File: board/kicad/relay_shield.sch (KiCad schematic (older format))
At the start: 16 parts

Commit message: Changed repository layout and added converted Eagle files.
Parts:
- removed R?: 10K, ~, symbol R
- removed R?: 220, ~, symbol R
- removed U?: Optoisolator, ~, symbol PHDARL
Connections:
- wire segments 35 -> 30
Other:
- moved on the sheet: R?, SW?
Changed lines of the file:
@@
 LIBS:contrib
 LIBS:valves
+LIBS:spark_core
 LIBS:relay_shield-cache
 EELAYER 27 0
@@
 Sheet 1 1
 Title ""
-Date "13 aug 2013"
+Date "14 aug 2013"
 Rev ""
 Comp ""
@@
 L SPST SW?
 U 1 1 520A9B3C
-P 1250 1400
-F 0 "SW?" H 1250 1500 70  0000 C CNN
-F 1 "SPST" H 1250 1300 70  0000 C CNN
-F 2 "~" H 1250 1400 60  0000 C CNN
-F 3 "~" H 1250 1400 60  0000 C CNN
-	1    1250 1400
+P 3000 1400
+F 0 "SW?" H 3000 1500 70  0000 C CNN
+F 1 "SPST" H 3000 1300 70  0000 C CNN
+F 2 "~" H 3000 1400 60  0000 C CNN
+F 3 "~" H 3000 1400 60  0000 C CNN
+	1    3000 1400
 	0    -1   -1   0
 $EndComp
@@
 L +3.3V #PWR04
 U 1 1 520A9BBE
-P 1250 900
-F 0 "#PWR04" H 1250 860 30  0001 C CNN
-F 1 "+3.3V" H 1250 1010 30  0000 C CNN
-F 2 "" H 1250 900 60  0000 C CNN
-F 3 "" H 1250 900 60  0000 C CNN
-	1    1250 900
+P 3000 900
+F 0 "#PWR04" H 3000 860 30  0001 C CNN
+F 1 "+3.3V" H 3000 1010 30  0000 C CNN
+F 2 "" H 3000 900 60  0000 C CNN
+F 3 "" H 3000 900 60  0000 C CNN
+	1    3000 900
 	1    0    0    -1
 $EndComp
@@
 	8450 5300 8700 5300
 Wire Wire Line
-	1250 1900 1250 2550
-Wire Wire Line
 	3350 900  3350 1450
 Wire Wire Line
 	3800 1300 3800 1450
-Wire Wire Line
-	3250 2550 3500 2550
 Wire Wire Line
 	3800 2350 3350 2350
@@
 Wire Wire Line
 	3800 1450 4200 1450
-Wire Wire Line
-	2750 1300 3800 1300
 $Comp
 L +5V #PWR07
@@
 L R R?
 U 1 1 520AA4F9
-P 3000 2550
-F 0 "R?" V 3080 2550 40  0000 C CNN
-F 1 "1K" V 3007 2551 40  0000 C CNN
-F 2 "~" V 2930 2550 30  0000 C CNN
-F 3 "~" H 3000 2550 30  0000 C CNN
-	1    3000 2550
+P 3250 2550
+F 0 "R?" V 3330 2550 40  0000 C CNN
+F 1 "1K" V 3257 2551 40  0000 C CNN
+F 2 "~" V 3180 2550 30  0000 C CNN
+F 3 "~" H 3250 2550 30  0000 C CNN
+	1    3250 2550
 	0    -1   -1   0
 $EndComp
-$Comp
-L PHDARL U?
-U 1 1 520AA563
-P 2150 2350
-F 0 "U?" H 2160 2670 70  0000 C CNN
-F 1 "Optoisolator" H 2160 2030 70  0000 C CNN
-F 2 "~" H 2150 2350 60  0000 C CNN
-F 3 "~" H 2150 2350 60  0000 C CNN
-	1    2150 2350
-	1    0    0    -1
-$EndComp
-Wire Wire Line
-	2750 1300 2750 2150
-Connection ~ 3350 1300
-$Comp
-L R R?
-U 1 1 520AA5CD
-P 1550 2800
-F 0 "R?" V 1630 2800 40  0000 C CNN
-F 1 "220" V 1557 2801 40  0000 C CNN
-F 2 "~" V 1480 2800 30  0000 C CNN
-F 3 "~" H 1550 2800 30  0000 C CNN
-	1    1550 2800
-	1    0    0    -1
-$EndComp
-Wire Wire Line
-	1250 2450 850  2450
 Text Notes 8750 4250 0    30   ~ 0
 MCP1825S 500 mA LDO\n
-Text Label 850  2150 0    60   ~ 0
+Text Label 2650 2550 0    60   ~ 0
 SS
-Text Label 850  2450 0    60   ~ 0
+Text Label 2650 2200 0    60   ~ 0
 RS
 $Comp
 L R R?
 U 1 1 520AAAED
-P 1250 2800
-F 0 "R?" V 1330 2800 40  0000 C CNN
-F 1 "10K" V 1257 2801 40  0000 C CNN
-F 2 "~" V 1180 2800 30  0000 C CNN
-F 3 "~" H 1250 2800 30  0000 C CNN
-	1    1250 2800
-	1    0    0    -1
-$EndComp
-Connection ~ 1250 2450
-$Comp
-L R R?
-U 1 1 520A9BFA
-P 3350 2800
-F 0 "R?" V 3430 2800 40  0000 C CNN
-F 1 "10K" V 3357 2801 40  0000 C CNN
-F 2 "~" V 3280 2800 30  0000 C CNN
-F 3 "~" H 3350 2800 30  0000 C CNN
-	1    3350 2800
-	1    0    0    -1
-$EndComp
-Wire Wire Line
-	1250 3200 3800 3200
-Wire Wire Line
-	3350 3050 3350 3200
-Connection ~ 3800 3200
-Wire Wire Line
-	1550 3200 1550 3050
-Connection ~ 3350 3200
-Wire Wire Line
-	1250 3200 1250 3050
-Connection ~ 1550 3200
-Wire Wire Line
-	850  2150 1550 2150
-Connection ~ 1250 2150
-Connection ~ 3350 2550
+P 3000 2800
+F 0 "R?" V 3080 2800 40  0000 C CNN
+F 1 "10K" V 3007 2801 40  0000 C CNN
+F 2 "~" V 2930 2800 30  0000 C CNN
+F 3 "~" H 3000 2800 30  0000 C CNN
+	1    3000 2800
+	1    0    0    -1
+$EndComp
 $Comp
 L CONN_2 P?
@@
 	1650 5200 1650 5300
 Connection ~ 1650 5200
-Text Notes 850  2550 0    60   ~ 0
+Text Notes 2650 2300 0    60   ~ 0
 <-
-Text Notes 850  2250 0    60   ~ 0
+Text Notes 2650 2650 0    60   ~ 0
 ->\n
+Wire Wire Line
+	3800 1300 3350 1300
+Connection ~ 3350 1300
+Wire Wire Line
+	3000 2550 3000 1900
+Wire Wire Line
+	3000 2550 2650 2550
+Wire Wire Line
+	3000 2200 2650 2200
+Connection ~ 3000 2200
+Wire Wire Line
+	3000 3050 3800 3050
+Connection ~ 3800 3050
 $EndSCHEMATC

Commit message: Finished schematic version 0.1.
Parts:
- added P2, P3, P5, P6, P7, P8: CONN_1, symbol CONN_1
- added P4: CT, symbol CONN_2
- added RE1: RELAY-JQX-15F, RELAY-JQX-15F, symbol RELAY-JQX-15F
- gave numbers to parts that had none: 13
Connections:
- no-connect marks 0 -> 7
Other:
- note added: "Current sensor"
- note added: "Mounting holes"
- note added: "Relay control"
- note added: "Spark Core"
- note added: "Support holes"
- note added: "ZIP tie for power cables"
- moved on the sheet: C1, D1, D2, P1, Q1, R1, R2, R3, R4, R5, R6, SW1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

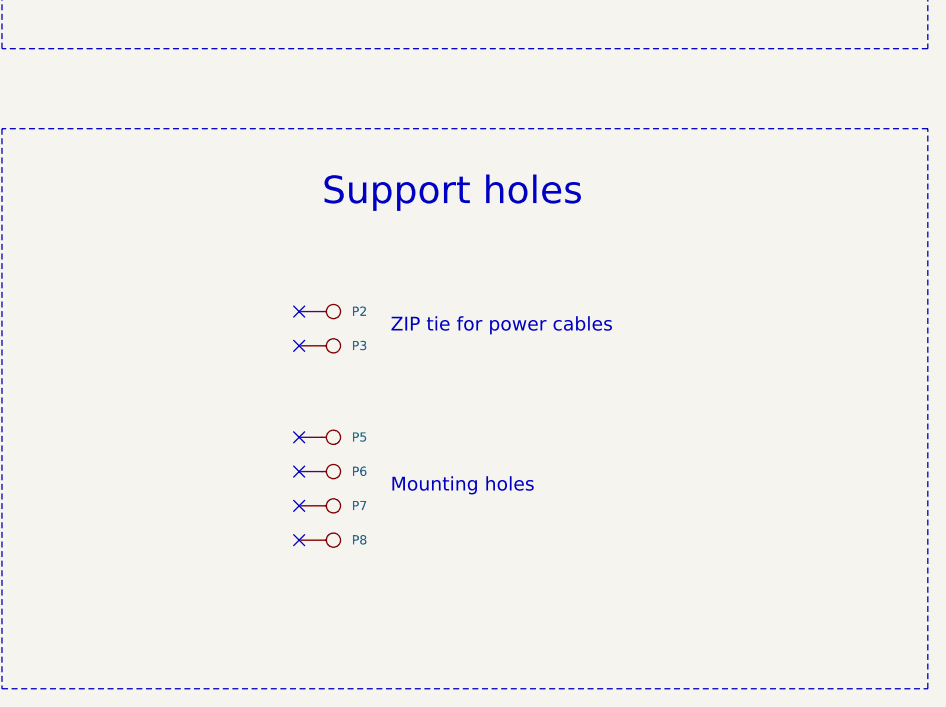
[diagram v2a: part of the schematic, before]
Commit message: Forgot to add a connector for power.
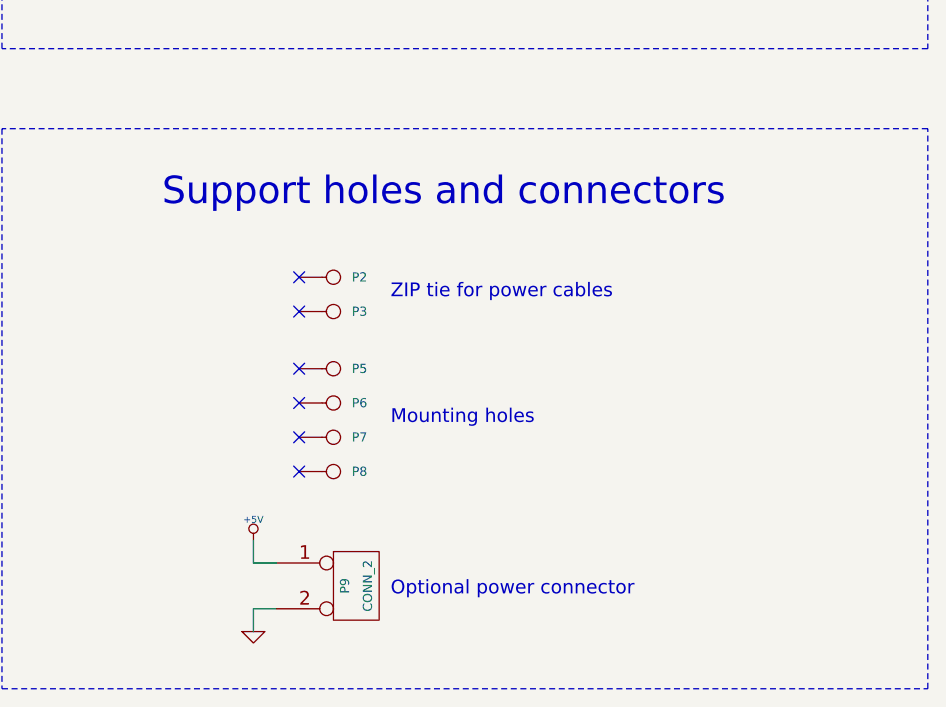
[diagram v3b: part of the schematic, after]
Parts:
- added P9: CONN_2, symbol CONN_2
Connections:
- wire segments 30 -> 34
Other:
- note added: "Optional power connector"
- note added: "Support holes and connectors"
- note removed: "Support holes"
- moved on the sheet: P2, P3, P5, P6, P7, P8
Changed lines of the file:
@@
 L CONN_1 P3
 U 1 1 520B3F18
-P 7250 5600
-F 0 "P3" H 7330 5600 40  0000 L CNN
-F 1 "CONN_1" H 7250 5655 30  0001 C CNN
-F 2 "" H 7250 5600 60  0000 C CNN
-F 3 "" H 7250 5600 60  0000 C CNN
-	1    7250 5600
-	1    0    0    -1
-$EndComp
-$Comp
-L CONN_1 P2
-U 1 1 520B3F25
 P 7250 5450
-F 0 "P2" H 7330 5450 40  0000 L CNN
+F 0 "P3" H 7330 5450 40  0000 L CNN
 F 1 "CONN_1" H 7250 5505 30  0001 C CNN
 F 2 "" H 7250 5450 60  0000 C CNN
@@
 $EndComp
 $Comp
+L CONN_1 P2
+U 1 1 520B3F25
+P 7250 5300
+F 0 "P2" H 7330 5300 40  0000 L CNN
+F 1 "CONN_1" H 7250 5355 30  0001 C CNN
+F 2 "" H 7250 5300 60  0000 C CNN
+F 3 "" H 7250 5300 60  0000 C CNN
+	1    7250 5300
+	1    0    0    -1
+$EndComp
+$Comp
 L CONN_1 P5
 U 1 1 520B41A3
+P 7250 5700
+F 0 "P5" H 7330 5700 40  0000 L CNN
+F 1 "CONN_1" H 7250 5755 30  0001 C CNN
+F 2 "" H 7250 5700 60  0000 C CNN
+F 3 "" H 7250 5700 60  0000 C CNN
+	1    7250 5700
+	1    0    0    -1
+$EndComp
+$Comp
+L CONN_1 P6
+U 1 1 520B41B0
+P 7250 5850
+F 0 "P6" H 7330 5850 40  0000 L CNN
+F 1 "CONN_1" H 7250 5905 30  0001 C CNN
+F 2 "" H 7250 5850 60  0000 C CNN
+F 3 "" H 7250 5850 60  0000 C CNN
+	1    7250 5850
+	1    0    0    -1
+$EndComp
+$Comp
+L CONN_1 P7
+U 1 1 520B41B6
 P 7250 6000
-F 0 "P5" H 7330 6000 40  0000 L CNN
+F 0 "P7" H 7330 6000 40  0000 L CNN
 F 1 "CONN_1" H 7250 6055 30  0001 C CNN
 F 2 "" H 7250 6000 60  0000 C CNN
@@
 $EndComp
 $Comp
-L CONN_1 P6
-U 1 1 520B41B0
+L CONN_1 P8
+U 1 1 520B41BC
 P 7250 6150
-F 0 "P6" H 7330 6150 40  0000 L CNN
+F 0 "P8" H 7330 6150 40  0000 L CNN
 F 1 "CONN_1" H 7250 6205 30  0001 C CNN
 F 2 "" H 7250 6150 60  0000 C CNN
@@
 	1    0    0    -1
 $EndComp
-$Comp
-L CONN_1 P7
-U 1 1 520B41B6
-P 7250 6300
-F 0 "P7" H 7330 6300 40  0000 L CNN
-F 1 "CONN_1" H 7250 6355 30  0001 C CNN
-F 2 "" H 7250 6300 60  0000 C CNN
-F 3 "" H 7250 6300 60  0000 C CNN
-	1    7250 6300
-	1    0    0    -1
-$EndComp
-$Comp
-L CONN_1 P8
-U 1 1 520B41BC
-P 7250 6450
-F 0 "P8" H 7330 6450 40  0000 L CNN
-F 1 "CONN_1" H 7250 6505 30  0001 C CNN
-F 2 "" H 7250 6450 60  0000 C CNN
-F 3 "" H 7250 6450 60  0000 C CNN
-	1    7250 6450
-	1    0    0    -1
-$EndComp
+NoConn ~ 7100 5300
 NoConn ~ 7100 5450
-NoConn ~ 7100 5600
+NoConn ~ 7100 5700
+NoConn ~ 7100 5850
 NoConn ~ 7100 6000
 NoConn ~ 7100 6150
-NoConn ~ 7100 6300
-NoConn ~ 7100 6450
-Text Notes 7500 5550 0    60   ~ 0
+Text Notes 7500 5400 0    60   ~ 0
 ZIP tie for power cables
-Text Notes 7500 6250 0    60   ~ 0
+Text Notes 7500 5950 0    60   ~ 0
 Mounting holes
-Text Notes 7200 5000 0    120  ~ 0
-Support holes
+Text Notes 6500 5000 0    120  ~ 0
+Support holes and connectors
 Text Notes 2450 5000 0    120  ~ 0
 Spark Core
@@
 Wire Notes Line
 	1500 4300 4850 4300
+$Comp
+L CONN_2 P9
+U 1 1 520B47A7
+P 7350 6650
+F 0 "P9" V 7300 6650 40  0000 C CNN
+F 1 "CONN_2" V 7400 6650 40  0000 C CNN
+F 2 "" H 7350 6650 60  0000 C CNN
+F 3 "" H 7350 6650 60  0000 C CNN
+	1    7350 6650
+	1    0    0    -1
+$EndComp
+$Comp
+L GND #PWR?
+U 1 1 520B47B6
+P 6900 6850
+F 0 "#PWR?" H 6900 6850 30  0001 C CNN
+F 1 "GND" H 6900 6780 30  0001 C CNN
+F 2 "" H 6900 6850 60  0000 C CNN
+F 3 "" H 6900 6850 60  0000 C CNN
+	1    6900 6850
+	1    0    0    -1
+$EndComp
+$Comp
+L +5V #PWR?
+U 1 1 520B47C5
+P 6900 6450
+F 0 "#PWR?" H 6900 6540 20  0001 C CNN
+F 1 "+5V" H 6900 6540 30  0000 C CNN
+F 2 "" H 6900 6450 60  0000 C CNN
+F 3 "" H 6900 6450 60  0000 C CNN
+	1    6900 6450
+	1    0    0    -1
+$EndComp
+Wire Wire Line
+	7000 6550 6900 6550
+Wire Wire Line
+	6900 6550 6900 6450
+Wire Wire Line
+	7000 6750 6900 6750
+Wire Wire Line
+	6900 6750 6900 6850
+Text Notes 7500 6700 0    60   ~ 0
+Optional power connector
 $EndSCHEMATC

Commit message: Base layout of the PCB.
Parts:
- P2: value CONN_1 -> Z1
- P3: value CONN_1 -> Z2
- P4: value CT -> AC
- P5: value CONN_1 -> MH1
- P6: value CONN_1 -> MH2
- P7: value CONN_1 -> MH3
- P8: value CONN_1 -> MH4
- P9: value CONN_2 -> PWR
- R3: value 18 - 1% -> 19.1
- SW1: value SPST -> SW
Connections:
- no-connect marks 7 -> 24
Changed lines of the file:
@@
 $EndComp
 $Comp
-L +3.3V #PWR5
+L +3.3V #PWR01
 U 1 1 5209DCD5
 P 3850 5250
-F 0 "#PWR5" H 3850 5210 30  0001 C CNN
+F 0 "#PWR01" H 3850 5210 30  0001 C CNN
 F 1 "+3.3V" H 3850 5360 30  0000 C CNN
 F 2 "" H 3850 5250 60  0000 C CNN
@@
 $EndComp
 $Comp
-L GND #PWR6
+L GND #PWR02
 U 1 1 5209DCE7
 P 3850 5700
-F 0 "#PWR6" H 3850 5700 30  0001 C CNN
+F 0 "#PWR02" H 3850 5700 30  0001 C CNN
 F 1 "GND" H 3850 5630 30  0001 C CNN
 F 2 "" H 3850 5700 60  0000 C CNN
@@
 $EndComp
 $Comp
-L GND #PWR2
+L GND #PWR03
 U 1 1 5209DD15
 P 2050 5500
-F 0 "#PWR2" H 2050 5500 30  0001 C CNN
+F 0 "#PWR03" H 2050 5500 30  0001 C CNN
 F 1 "GND" H 2050 5430 30  0001 C CNN
 F 2 "" H 2050 5500 60  0000 C CNN
@@
 P 6750 1850
 F 0 "SW1" H 6750 1950 70  0000 C CNN
-F 1 "SPST" H 6750 1750 70  0000 C CNN
+F 1 "SW" H 6750 1750 70  0000 C CNN
 F 2 "~" H 6750 1850 60  0000 C CNN
 F 3 "~" H 6750 1850 60  0000 C CNN
@@
 $EndComp
 $Comp
-L +3.3V #PWR7
+L +3.3V #PWR04
 U 1 1 520A9BBE
 P 6750 1350
-F 0 "#PWR7" H 6750 1310 30  0001 C CNN
+F 0 "#PWR04" H 6750 1310 30  0001 C CNN
 F 1 "+3.3V" H 6750 1460 30  0000 C CNN
 F 2 "" H 6750 1350 60  0000 C CNN
@@
 $EndComp
 $Comp
-L GND #PWR9
+L GND #PWR05
 U 1 1 520A9BCD
 P 7550 3700
-F 0 "#PWR9" H 7550 3700 30  0001 C CNN
+F 0 "#PWR05" H 7550 3700 30  0001 C CNN
 F 1 "GND" H 7550 3630 30  0001 C CNN
 F 2 "" H 7550 3700 60  0000 C CNN
@@
 $EndComp
 $Comp
-L +5V #PWR1
+L +5V #PWR06
 U 1 1 520AA096
 P 2050 5250
-F 0 "#PWR1" H 2050 5340 20  0001 C CNN
+F 0 "#PWR06" H 2050 5340 20  0001 C CNN
 F 1 "+5V" H 2050 5340 30  0000 C CNN
 F 2 "" H 2050 5250 60  0000 C CNN
@@
 $EndComp
 $Comp
-L +5V #PWR8
+L +5V #PWR07
 U 1 1 520AA26A
 P 7100 1350
-F 0 "#PWR8" H 7100 1440 20  0001 C CNN
+F 0 "#PWR07" H 7100 1440 20  0001 C CNN
 F 1 "+5V" H 7100 1440 30  0000 C CNN
 F 2 "" H 7100 1350 60  0000 C CNN
@@
 P 3150 2150
 F 0 "R3" V 3230 2150 40  0000 C CNN
-F 1 "18 - 1%" V 3157 2151 40  0000 C CNN
+F 1 "19.1" V 3157 2151 40  0000 C CNN
 F 2 "~" V 3080 2150 30  0000 C CNN
 F 3 "~" H 3150 2150 30  0000 C CNN
@@
 CS
 $Comp
-L +3.3V #PWR3
+L +3.3V #PWR08
 U 1 1 520AADB5
 P 2750 1900
-F 0 "#PWR3" H 2750 1860 30  0001 C CNN
+F 0 "#PWR08" H 2750 1860 30  0001 C CNN
 F 1 "+3.3V" H 2750 2010 30  0000 C CNN
 F 2 "" H 2750 1900 60  0000 C CNN
@@
 $EndComp
 $Comp
-L GND #PWR4
+L GND #PWR09
 U 1 1 520AAF06
 P 2950 3000
-F 0 "#PWR4" H 2950 3000 30  0001 C CNN
+F 0 "#PWR09" H 2950 3000 30  0001 C CNN
 F 1 "GND" H 2950 2930 30  0001 C CNN
 F 2 "" H 2950 3000 60  0000 C CNN
@@
 P 9500 2200
 F 0 "P4" V 9450 2200 40  0000 C CNN
-F 1 "CT" V 9550 2200 40  0000 C CNN
+F 1 "AC" V 9550 2200 40  0000 C CNN
 F 2 "" H 9500 2200 60  0000 C CNN
 F 3 "" H 9500 2200 60  0000 C CNN
@@
 P 7250 5450
 F 0 "P3" H 7330 5450 40  0000 L CNN
-F 1 "CONN_1" H 7250 5505 30  0001 C CNN
+F 1 "Z2" H 7250 5505 30  0001 C CNN
 F 2 "" H 7250 5450 60  0000 C CNN
 F 3 "" H 7250 5450 60  0000 C CNN
@@
 P 7250 5300
 F 0 "P2" H 7330 5300 40  0000 L CNN
-F 1 "CONN_1" H 7250 5355 30  0001 C CNN
+F 1 "Z1" H 7250 5355 30  0001 C CNN
 F 2 "" H 7250 5300 60  0000 C CNN
 F 3 "" H 7250 5300 60  0000 C CNN
@@
 P 7250 5700
 F 0 "P5" H 7330 5700 40  0000 L CNN
-F 1 "CONN_1" H 7250 5755 30  0001 C CNN
+F 1 "MH1" H 7250 5755 30  0001 C CNN
 F 2 "" H 7250 5700 60  0000 C CNN
 F 3 "" H 7250 5700 60  0000 C CNN
@@
 P 7250 5850
 F 0 "P6" H 7330 5850 40  0000 L CNN
-F 1 "CONN_1" H 7250 5905 30  0001 C CNN
+F 1 "MH2" H 7250 5905 30  0001 C CNN
 F 2 "" H 7250 5850 60  0000 C CNN
 F 3 "" H 7250 5850 60  0000 C CNN
@@
 P 7250 6000
 F 0 "P7" H 7330 6000 40  0000 L CNN
-F 1 "CONN_1" H 7250 6055 30  0001 C CNN
+F 1 "MH3" H 7250 6055 30  0001 C CNN
 F 2 "" H 7250 6000 60  0000 C CNN
 F 3 "" H 7250 6000 60  0000 C CNN
@@
 P 7250 6150
 F 0 "P8" H 7330 6150 40  0000 L CNN
-F 1 "CONN_1" H 7250 6205 30  0001 C CNN
+F 1 "MH4" H 7250 6205 30  0001 C CNN
 F 2 "" H 7250 6150 60  0000 C CNN
 F 3 "" H 7250 6150 60  0000 C CNN
@@
 P 7350 6650
 F 0 "P9" V 7300 6650 40  0000 C CNN
-F 1 "CONN_2" V 7400 6650 40  0000 C CNN
+F 1 "PWR" V 7400 6650 40  0000 C CNN
 F 2 "" H 7350 6650 60  0000 C CNN
 F 3 "" H 7350 6650 60  0000 C CNN
@@
 $EndComp
 $Comp
-L GND #PWR?
+L GND #PWR010
 U 1 1 520B47B6
 P 6900 6850
-F 0 "#PWR?" H 6900 6850 30  0001 C CNN
+F 0 "#PWR010" H 6900 6850 30  0001 C CNN
 F 1 "GND" H 6900 6780 30  0001 C CNN
 F 2 "" H 6900 6850 60  0000 C CNN
@@
 $EndComp
 $Comp
-L +5V #PWR?
+L +5V #PWR011
 U 1 1 520B47C5
 P 6900 6450
-F 0 "#PWR?" H 6900 6540 20  0001 C CNN
+F 0 "#PWR011" H 6900 6540 20  0001 C CNN
 F 1 "+5V" H 6900 6540 30  0000 C CNN
 F 2 "" H 6900 6450 60  0000 C CNN
@@
 $EndComp
 Wire Wire Line
-	7000 6550 6900 6550
+	6650 6550 7000 6550
 Wire Wire Line
 	6900 6550 6900 6450
 Wire Wire Line
-	7000 6750 6900 6750
+	6450 6750 7000 6750
 Wire Wire Line
 	6900 6750 6900 6850
 Text Notes 7500 6700 0    60   ~ 0
 Optional power connector
+NoConn ~ 3600 6250
+NoConn ~ 3600 6150
+NoConn ~ 3600 6050
+NoConn ~ 3600 5950
+NoConn ~ 3600 5850
+NoConn ~ 3600 5750
+NoConn ~ 3600 5550
+NoConn ~ 3600 5450
+NoConn ~ 2300 5550
+NoConn ~ 2300 5650
+NoConn ~ 2300 5750
+NoConn ~ 2300 5850
+NoConn ~ 2300 5950
+NoConn ~ 2300 6050
+NoConn ~ 2300 6150
+NoConn ~ 2300 6250
+NoConn ~ 2300 6350
+$Comp
+L PWR_FLAG #FLG012
+U 1 1 520BD335
+P 6650 6550
+F 0 "#FLG012" H 6650 6645 30  0001 C CNN
+F 1 "PWR_FLAG" H 6650 6730 30  0000 C CNN
+F 2 "" H 6650 6550 60  0000 C CNN
+F 3 "" H 6650 6550 60  0000 C CNN
+	1    6650 6550
+	1    0    0    -1
+$EndComp
+$Comp
+L PWR_FLAG #FLG013
+U 1 1 520BD344
+P 6450 6750
+F 0 "#FLG013" H 6450 6845 30  0001 C CNN
+F 1 "PWR_FLAG" H 6450 6930 30  0000 C CNN
+F 2 "" H 6450 6750 60  0000 C CNN
+F 3 "" H 6450 6750 60  0000 C CNN
+	1    6450 6750
+	1    0    0    -1
+$EndComp
+Connection ~ 6900 6550
+Connection ~ 6900 6750
+$Comp
+L PWR_FLAG #FLG014
+U 1 1 520BD3C6
+P 3600 5350
+F 0 "#FLG014" H 3600 5445 30  0001 C CNN
+F 1 "PWR_FLAG" H 3600 5530 30  0000 C CNN
+F 2 "" H 3600 5350 60  0000 C CNN
+F 3 "" H 3600 5350 60  0000 C CNN
+	1    3600 5350
+	1    0    0    -1
+$EndComp
 $EndSCHEMATC
